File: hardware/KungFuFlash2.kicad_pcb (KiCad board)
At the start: 2 copper layers, 60.6 x 62 mm, 53 parts, among them J1 SWD, J2 USB_B_Micro, J3 Wifi, Q1 BC817, SW1 Reset, SW2 Menu, SW3 Special, U1 C64-Exp-Port, U2 AMS1117-3.3, U3 STM32H7B0VBTx, Y1 25MHz

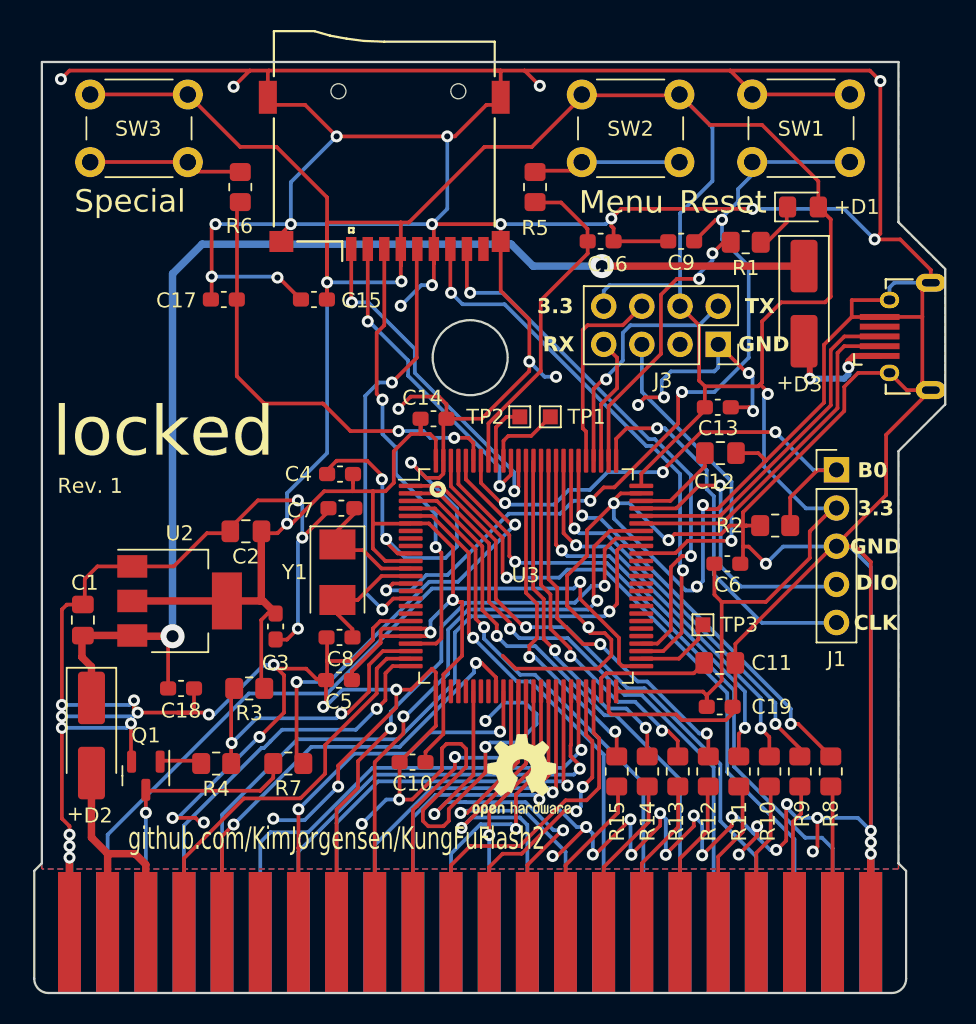
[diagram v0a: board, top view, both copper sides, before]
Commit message: added USB-C connector
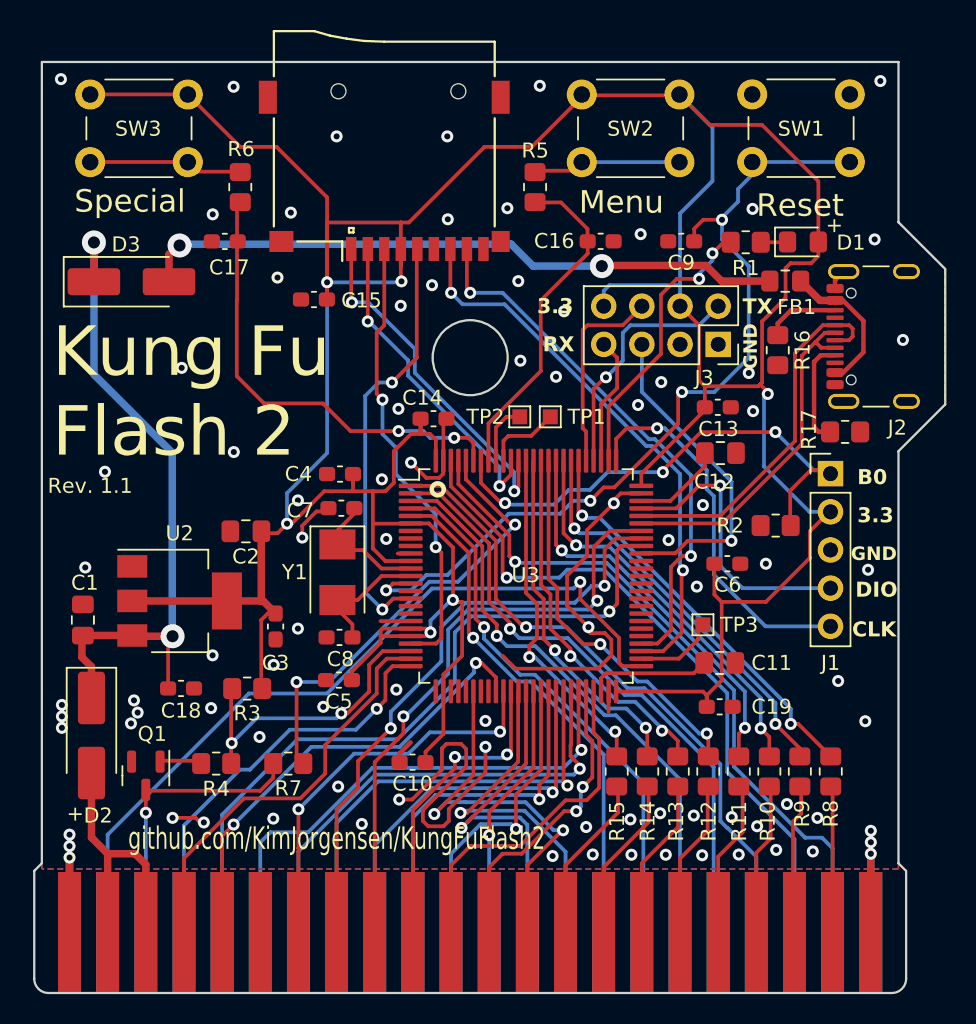
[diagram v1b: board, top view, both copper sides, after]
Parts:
- removed REF**: OSHW-Logo2_7.3x6mm_SilkScreen, Symbol:OSHW-Logo2_7.3x6mm_SilkScreen
- added FB1: FerriteBead, Inductor_SMD:L_0805_2012Metric_Pad1.15x1.40mm_HandSolder, F.Cu at (125.9, 82.8)
- added R16: 5k1, Resistor_SMD:R_0805_2012Metric_Pad1.20x1.40mm_HandSolder, F.Cu at (125.4, 87.4)
- added R17: 5k1, Resistor_SMD:R_0805_2012Metric_Pad1.20x1.40mm_HandSolder, F.Cu at (129.9, 92.8)
- D2, D3: value D_Schottky -> SS14
- J2: value USB_B_Micro -> USB_C_Plug_USB2.0; footprint KungFuFlash2:Conn_USBmicro-B_ebay-side_TH -> Connector_USB:USB_C_Receptacle_GCT_USB4105-xx-A_16P_TopMnt_Horizontal
- moved D3 44.8 mm to (82.4, 82.8), turned to 0 degrees
- moved C17 3.87 mm to (88.6, 80.1)
- moved J2 2.69 mm to (132.9, 86.5)
- moved D1 2.33 mm to (127.1, 80.2)
- moved J1 0.47 mm to (128.9, 95.6)
- moved R3 0.13 mm to (90.1, 109.9)
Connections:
- net +5V renamed +5V_Cartridge
- D3 pad 2: +5C -> +5V_USB
- U3 pad 70: /USB_DM -> /USB_D_M
- U3 pad 71: /USB_DP -> /USB_D_P
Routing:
- net GND: track 705.4 -> 93.1 mm, vias 77 -> 87
- net +5V_USB: track 0.00 -> 43.2 mm, vias 0 -> 2
- net Net-(D2-K): track 81.4 -> 44.9 mm
- net /USB_D_P: track 0.00 -> 24.7 mm
- net /USB_D_M: track 0.00 -> 23.0 mm
- net /USB_DP: track 23.0 -> 0.00 mm
- net /USB_DM: track 22.9 -> 0.00 mm
- net Net-(FB1-Pad1): track 0.00 -> 9.82 mm
- net +5C: track 7.91 -> 0.00 mm, vias 2 -> 0
- net Net-(J2-CC): track 0.00 -> 7.13 mm
- net Net-(J2-VCONN): track 0.00 -> 4.96 mm
- net +3V3: track 276.9 -> 275.0 mm
- net Net-(D1-K): track 2.90 -> 1.79 mm
- net /~{RST}: track 56.2 -> 56.7 mm
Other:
- board text added: "Kung Fu Flash 2"
- board text added: "Rev. 1.1"
- board text removed: "Rev. 1"
- board text removed: "locked"
